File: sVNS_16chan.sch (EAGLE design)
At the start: 56 parts, among them IC2 OPA990IDCKR, IC3 EFM8SB10F8A-A-QFN24EFM8SB10F8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, J1 M50-3631042, J2 M50-3631042, J3 M50-3631042, U1 NT3H2211W0FHKH, U2 LT8410EDC-1#TRMPBF, U3 MUX36S16IRSNR, U4 MUX36S16IRSNR

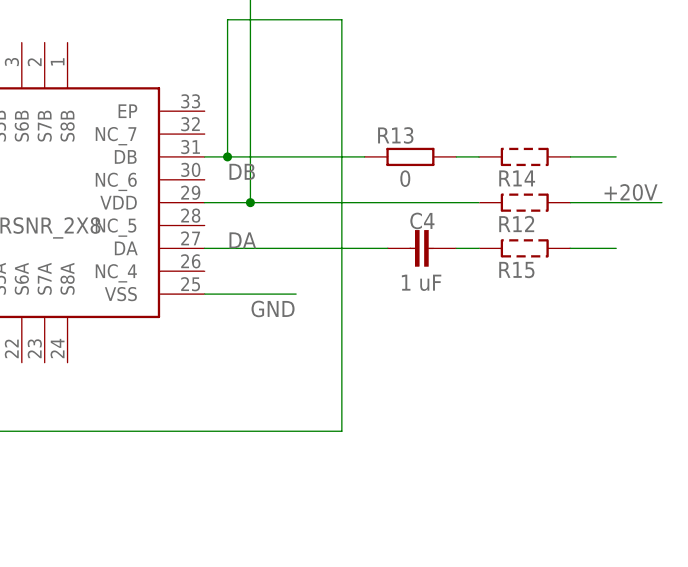
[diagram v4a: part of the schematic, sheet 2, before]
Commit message: Checkpoint 1. Output capacitor changed to 10 uF, form factor 0603.
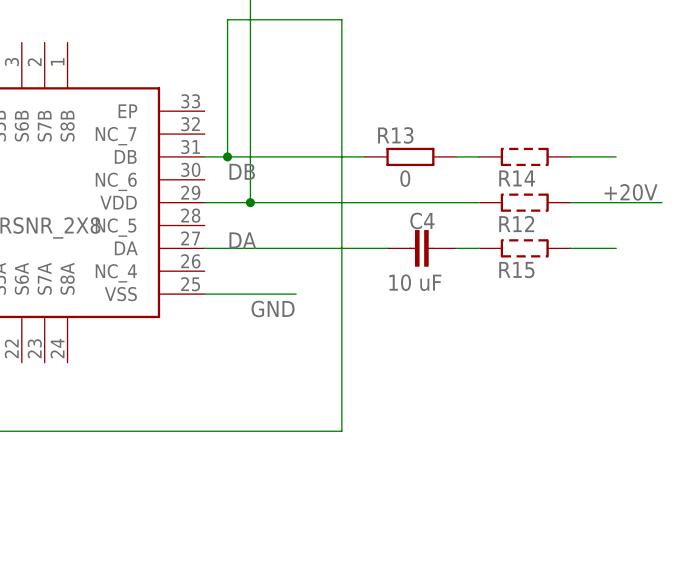
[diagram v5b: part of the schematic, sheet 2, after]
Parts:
- C4: value 1 uF -> 10 uF; device rcl:C-EUC0402 -> rcl:C-EUC0603
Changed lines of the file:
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@@
 <grid distance="0.1" unitdist="inch" unit="inch" style="lines" multiple="1" display="no" altdistance="0.01" altunitdist="inch" altunit="inch"/>
 <layers>
-<layer number="1" name="Top" color="4" fill="1" visible="no" active="no"/>
-<layer number="2" name="Route2" color="16" fill="1" visible="no" active="no"/>
-<layer number="3" name="Route3" color="17" fill="1" visible="no" active="no"/>
-<layer number="4" name="Route4" color="18" fill="1" visible="no" active="no"/>
-<layer number="5" name="Route5" color="19" fill="1" visible="no" active="no"/>
-<layer number="6" name="Route6" color="25" fill="1" visible="no" active="no"/>
-<layer number="7" name="Route7" color="26" fill="1" visible="no" active="no"/>
-<layer number="8" name="Route8" color="27" fill="1" visible="no" active="no"/>
-<layer number="9" name="Route9" color="28" fill="1" visible="no" active="no"/>
-<layer number="10" name="Route10" color="29" fill="1" visible="no" active="no"/>
-<layer number="11" name="Route11" color="30" fill="1" visible="no" active="no"/>
-<layer number="12" name="Route12" color="20" fill="1" visible="no" active="no"/>
-<layer number="13" name="Route13" color="21" fill="1" visible="no" active="no"/>
-<layer number="14" name="Route14" color="22" fill="1" visible="no" active="no"/>
-<layer number="15" name="Route15" color="23" fill="1" visible="no" active="no"/>
-<layer number="16" name="Bottom" color="1" fill="1" visible="no" active="no"/>
-<layer number="17" name="Pads" color="2" fill="1" visible="no" active="no"/>
-<layer number="18" name="Vias" color="2" fill="1" visible="no" active="no"/>
-<layer number="19" name="Unrouted" color="6" fill="1" visible="no" active="no"/>
-<layer number="20" name="Dimension" color="24" fill="1" visible="no" active="no"/>
-<layer number="21" name="tPlace" color="7" fill="1" visible="no" active="no"/>
-<layer number="22" name="bPlace" color="7" fill="1" visible="no" active="no"/>
-<layer number="23" name="tOrigins" color="15" fill="1" visible="no" active="no"/>
-<layer number="24" name="bOrigins" color="15" fill="1" visible="no" active="no"/>
-<layer number="25" name="tNames" color="7" fill="1" visible="no" active="no"/>
-<layer number="26" name="bNames" color="7" fill="1" visible="no" active="no"/>
-<layer number="27" name="tValues" color="7" fill="1" visible="no" active="no"/>
-<layer number="28" name="bValues" color="7" fill="1" visible="no" active="no"/>
+<layer number="1" name="Top" color="4" fill="1" visible="yes" active="no"/>
+<layer number="2" name="Route2" color="16" fill="1" visible="yes" active="no"/>
+<layer number="3" name="Route3" color="17" fill="1" visible="yes" active="no"/>
+<layer number="4" name="Route4" color="18" fill="1" visible="yes" active="no"/>
+<layer number="5" name="Route5" color="19" fill="1" visible="yes" active="no"/>
+<layer number="6" name="Route6" color="25" fill="1" visible="yes" active="no"/>
+<layer number="7" name="Route7" color="26" fill="1" visible="yes" active="no"/>
+<layer number="8" name="Route8" color="27" fill="1" visible="yes" active="no"/>
+<layer number="9" name="Route9" color="28" fill="1" visible="yes" active="no"/>
+<layer number="10" name="Route10" color="29" fill="1" visible="yes" active="no"/>
+<layer number="11" name="Route11" color="30" fill="1" visible="yes" active="no"/>
+<layer number="12" name="Route12" color="20" fill="1" visible="yes" active="no"/>
+<layer number="13" name="Route13" color="21" fill="1" visible="yes" active="no"/>
+<layer number="14" name="Route14" color="22" fill="1" visible="yes" active="no"/>
+<layer number="15" name="Route15" color="23" fill="1" visible="yes" active="no"/>
+<layer number="16" name="Bottom" color="1" fill="1" visible="yes" active="no"/>
+<layer number="17" name="Pads" color="2" fill="1" visible="yes" active="no"/>
+<layer number="18" name="Vias" color="2" fill="1" visible="yes" active="no"/>
+<layer number="19" name="Unrouted" color="6" fill="1" visible="yes" active="no"/>
+<layer number="20" name="Dimension" color="24" fill="1" visible="yes" active="no"/>
+<layer number="21" name="tPlace" color="7" fill="1" visible="yes" active="no"/>
+<layer number="22" name="bPlace" color="7" fill="1" visible="yes" active="no"/>
+<layer number="23" name="tOrigins" color="15" fill="1" visible="yes" active="no"/>
+<layer number="24" name="bOrigins" color="15" fill="1" visible="yes" active="no"/>
+<layer number="25" name="tNames" color="7" fill="1" visible="yes" active="no"/>
+<layer number="26" name="bNames" color="7" fill="1" visible="yes" active="no"/>
+<layer number="27" name="tValues" color="7" fill="1" visible="yes" active="no"/>
+<layer number="28" name="bValues" color="7" fill="1" visible="yes" active="no"/>
 <layer number="29" name="tStop" color="7" fill="3" visible="no" active="no"/>
 <layer number="30" name="bStop" color="7" fill="6" visible="no" active="no"/>
@@
 <layer number="35" name="tGlue" color="7" fill="4" visible="no" active="no"/>
 <layer number="36" name="bGlue" color="7" fill="5" visible="no" active="no"/>
-<layer number="37" name="tTest" color="7" fill="1" visible="no" active="no"/>
-<layer number="38" name="bTest" color="7" fill="1" visible="no" active="no"/>
+<layer number="37" name="tTest" color="7" fill="1" visible="yes" active="no"/>
+<layer number="38" name="bTest" color="7" fill="1" visible="yes" active="no"/>
 <layer number="39" name="tKeepout" color="4" fill="11" visible="no" active="no"/>
 <layer number="40" name="bKeepout" color="1" fill="11" visible="no" active="no"/>
@@
 <layer number="44" name="Drills" color="7" fill="1" visible="no" active="no"/>
 <layer number="45" name="Holes" color="7" fill="1" visible="no" active="no"/>
-<layer number="46" name="Milling" color="3" fill="1" visible="no" active="no"/>
-<layer number="47" name="Measures" color="7" fill="1" visible="no" active="no"/>
-<layer number="48" name="Document" color="7" fill="1" visible="no" active="no"/>
-<layer number="49" name="Reference" color="7" fill="1" visible="no" active="no"/>
-<layer number="50" name="dxf" color="7" fill="1" visible="no" active="no"/>
-<layer number="51" name="tDocu" color="7" fill="1" visible="no" active="no"/>
-<layer number="52" name="bDocu" color="7" fill="1" visible="no" active="no"/>
-<layer number="53" name="tGND_GNDA" color="7" fill="9" visible="no" active="no"/>
-<layer number="54" name="bGND_GNDA" color="1" fill="9" visible="no" active="no"/>
-<layer number="56" name="wert" color="7" fill="1" visible="no" active="no"/>
-<layer number="57" name="tCAD" color="7" fill="1" visible="no" active="no"/>
-<layer number="59" name="tCarbon" color="7" fill="1" visible="no" active="no"/>
-<layer number="60" name="bCarbon" color="7" fill="1" visible="no" active="no"/>
+<layer number="46" name="Milling" color="3" fill="1" visible="yes" active="no"/>
+<layer number="47" name="Measures" color="7" fill="1" visible="yes" active="no"/>
+<layer number="48" name="Document" color="7" fill="1" visible="yes" active="no"/>
+<layer number="49" name="Reference" color="7" fill="1" visible="yes" active="no"/>
+<layer number="50" name="dxf" color="7" fill="1" visible="yes" active="no"/>
+<layer number="51" name="tDocu" color="7" fill="1" visible="yes" active="no"/>
+<layer number="52" name="bDocu" color="7" fill="1" visible="yes" active="no"/>
+<layer number="53" name="tGND_GNDA" color="7" fill="9" visible="yes" active="no"/>
+<layer number="54" name="bGND_GNDA" color="1" fill="9" visible="yes" active="no"/>
+<layer number="56" name="wert" color="7" fill="1" visible="yes" active="no"/>
+<layer number="57" name="tCAD" color="7" fill="1" visible="yes" active="no"/>
+<layer number="59" name="tCarbon" color="7" fill="1" visible="yes" active="no"/>
+<layer number="60" name="bCarbon" color="7" fill="1" visible="yes" active="no"/>
 <layer number="88" name="SimResults" color="9" fill="1" visible="yes" active="yes"/>
 <layer number="89" name="SimProbes" color="9" fill="1" visible="yes" active="yes"/>
@@
 <part name="R10" library="rcl" library_urn="urn:adsk.eagle:library:334" deviceset="R-EU_" device="R0402" package3d_urn="urn:adsk.eagle:package:23547/3" value="220k"/>
 <part name="C12" library="rcl" library_urn="urn:adsk.eagle:library:334" deviceset="C-EU" device="C0402" package3d_urn="urn:adsk.eagle:package:23626/2" value="0.1 uF"/>
-<part name="C4" library="rcl" library_urn="urn:adsk.eagle:library:334" deviceset="C-EU" device="C0402" package3d_urn="urn:adsk.eagle:package:23626/2" value="1 uF"/>
+<part name="C4" library="rcl" library_urn="urn:adsk.eagle:library:334" deviceset="C-EU" device="C0603" package3d_urn="urn:adsk.eagle:package:23616/2" value="10 uF"/>
 <part name="R13" library="rcl" library_urn="urn:adsk.eagle:library:334" deviceset="R-EU_" device="R0402" package3d_urn="urn:adsk.eagle:package:23547/3" value="0"/>
 <part name="C11" library="rcl" library_urn="urn:adsk.eagle:library:334" deviceset="C-EU" device="C0402" package3d_urn="urn:adsk.eagle:package:23626/2" value="0.1 uF"/>

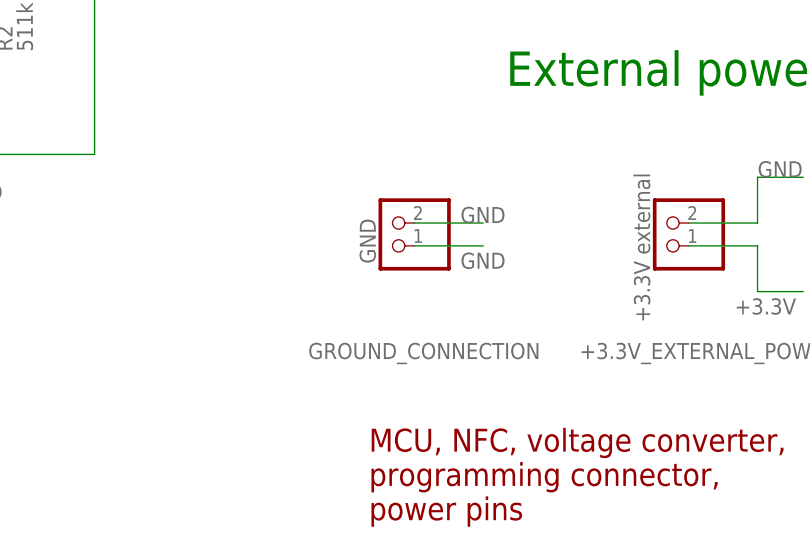
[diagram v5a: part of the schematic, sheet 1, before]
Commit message: Checkpoint 2. Minor changes and optimizations for the manufacturing. Output cap changed to 10 uF. Prepared for PCBway if this version considered to be manufactured.
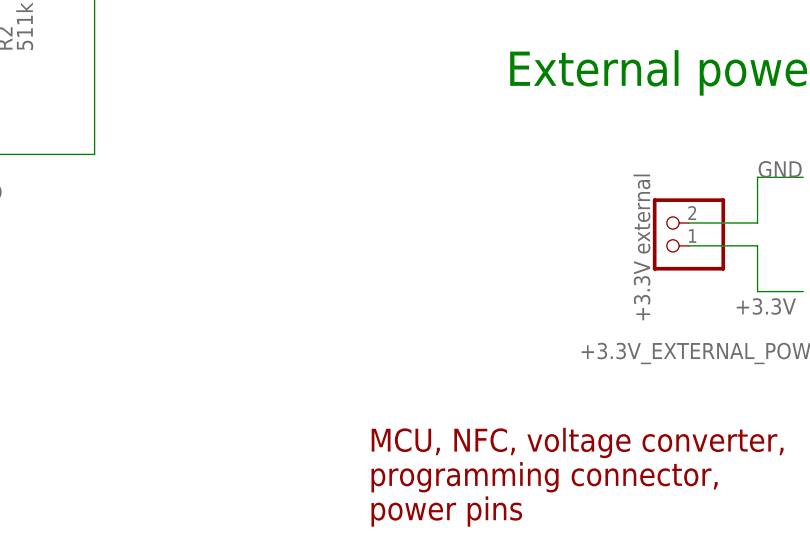
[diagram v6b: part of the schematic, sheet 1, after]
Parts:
- removed GROUND_CONNECTION: GND, pinhead:PINHD-1X2
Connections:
- net GND: no longer GROUND_CONNECTION.1, GROUND_CONNECTION.2
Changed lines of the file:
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@@
 <grid distance="0.1" unitdist="inch" unit="inch" style="lines" multiple="1" display="no" altdistance="0.01" altunitdist="inch" altunit="inch"/>
 <layers>
-<layer number="1" name="Top" color="4" fill="1" visible="yes" active="no"/>
-<layer number="2" name="Route2" color="16" fill="1" visible="yes" active="no"/>
-<layer number="3" name="Route3" color="17" fill="1" visible="yes" active="no"/>
-<layer number="4" name="Route4" color="18" fill="1" visible="yes" active="no"/>
-<layer number="5" name="Route5" color="19" fill="1" visible="yes" active="no"/>
-<layer number="6" name="Route6" color="25" fill="1" visible="yes" active="no"/>
-<layer number="7" name="Route7" color="26" fill="1" visible="yes" active="no"/>
-<layer number="8" name="Route8" color="27" fill="1" visible="yes" active="no"/>
-<layer number="9" name="Route9" color="28" fill="1" visible="yes" active="no"/>
-<layer number="10" name="Route10" color="29" fill="1" visible="yes" active="no"/>
-<layer number="11" name="Route11" color="30" fill="1" visible="yes" active="no"/>
-<layer number="12" name="Route12" color="20" fill="1" visible="yes" active="no"/>
-<layer number="13" name="Route13" color="21" fill="1" visible="yes" active="no"/>
-<layer number="14" name="Route14" color="22" fill="1" visible="yes" active="no"/>
-<layer number="15" name="Route15" color="23" fill="1" visible="yes" active="no"/>
-<layer number="16" name="Bottom" color="1" fill="1" visible="yes" active="no"/>
-<layer number="17" name="Pads" color="2" fill="1" visible="yes" active="no"/>
-<layer number="18" name="Vias" color="2" fill="1" visible="yes" active="no"/>
-<layer number="19" name="Unrouted" color="6" fill="1" visible="yes" active="no"/>
-<layer number="20" name="Dimension" color="24" fill="1" visible="yes" active="no"/>
-<layer number="21" name="tPlace" color="7" fill="1" visible="yes" active="no"/>
-<layer number="22" name="bPlace" color="7" fill="1" visible="yes" active="no"/>
-<layer number="23" name="tOrigins" color="15" fill="1" visible="yes" active="no"/>
-<layer number="24" name="bOrigins" color="15" fill="1" visible="yes" active="no"/>
-<layer number="25" name="tNames" color="7" fill="1" visible="yes" active="no"/>
-<layer number="26" name="bNames" color="7" fill="1" visible="yes" active="no"/>
-<layer number="27" name="tValues" color="7" fill="1" visible="yes" active="no"/>
-<layer number="28" name="bValues" color="7" fill="1" visible="yes" active="no"/>
+<layer number="1" name="Top" color="4" fill="1" visible="no" active="no"/>
+<layer number="2" name="Route2" color="16" fill="1" visible="no" active="no"/>
+<layer number="3" name="Route3" color="17" fill="1" visible="no" active="no"/>
+<layer number="4" name="Route4" color="18" fill="1" visible="no" active="no"/>
+<layer number="5" name="Route5" color="19" fill="1" visible="no" active="no"/>
+<layer number="6" name="Route6" color="25" fill="1" visible="no" active="no"/>
+<layer number="7" name="Route7" color="26" fill="1" visible="no" active="no"/>
+<layer number="8" name="Route8" color="27" fill="1" visible="no" active="no"/>
+<layer number="9" name="Route9" color="28" fill="1" visible="no" active="no"/>
+<layer number="10" name="Route10" color="29" fill="1" visible="no" active="no"/>
+<layer number="11" name="Route11" color="30" fill="1" visible="no" active="no"/>
+<layer number="12" name="Route12" color="20" fill="1" visible="no" active="no"/>
+<layer number="13" name="Route13" color="21" fill="1" visible="no" active="no"/>
+<layer number="14" name="Route14" color="22" fill="1" visible="no" active="no"/>
+<layer number="15" name="Route15" color="23" fill="1" visible="no" active="no"/>
+<layer number="16" name="Bottom" color="1" fill="1" visible="no" active="no"/>
+<layer number="17" name="Pads" color="2" fill="1" visible="no" active="no"/>
+<layer number="18" name="Vias" color="2" fill="1" visible="no" active="no"/>
+<layer number="19" name="Unrouted" color="6" fill="1" visible="no" active="no"/>
+<layer number="20" name="Dimension" color="24" fill="1" visible="no" active="no"/>
+<layer number="21" name="tPlace" color="7" fill="1" visible="no" active="no"/>
+<layer number="22" name="bPlace" color="7" fill="1" visible="no" active="no"/>
+<layer number="23" name="tOrigins" color="15" fill="1" visible="no" active="no"/>
+<layer number="24" name="bOrigins" color="15" fill="1" visible="no" active="no"/>
+<layer number="25" name="tNames" color="7" fill="1" visible="no" active="no"/>
+<layer number="26" name="bNames" color="7" fill="1" visible="no" active="no"/>
+<layer number="27" name="tValues" color="7" fill="1" visible="no" active="no"/>
+<layer number="28" name="bValues" color="7" fill="1" visible="no" active="no"/>
 <layer number="29" name="tStop" color="7" fill="3" visible="no" active="no"/>
 <layer number="30" name="bStop" color="7" fill="6" visible="no" active="no"/>
@@
 <layer number="35" name="tGlue" color="7" fill="4" visible="no" active="no"/>
 <layer number="36" name="bGlue" color="7" fill="5" visible="no" active="no"/>
-<layer number="37" name="tTest" color="7" fill="1" visible="yes" active="no"/>
-<layer number="38" name="bTest" color="7" fill="1" visible="yes" active="no"/>
+<layer number="37" name="tTest" color="7" fill="1" visible="no" active="no"/>
+<layer number="38" name="bTest" color="7" fill="1" visible="no" active="no"/>
 <layer number="39" name="tKeepout" color="4" fill="11" visible="no" active="no"/>
 <layer number="40" name="bKeepout" color="1" fill="11" visible="no" active="no"/>
@@
 <layer number="44" name="Drills" color="7" fill="1" visible="no" active="no"/>
 <layer number="45" name="Holes" color="7" fill="1" visible="no" active="no"/>
-<layer number="46" name="Milling" color="3" fill="1" visible="yes" active="no"/>
-<layer number="47" name="Measures" color="7" fill="1" visible="yes" active="no"/>
-<layer number="48" name="Document" color="7" fill="1" visible="yes" active="no"/>
-<layer number="49" name="Reference" color="7" fill="1" visible="yes" active="no"/>
-<layer number="50" name="dxf" color="7" fill="1" visible="yes" active="no"/>
-<layer number="51" name="tDocu" color="7" fill="1" visible="yes" active="no"/>
-<layer number="52" name="bDocu" color="7" fill="1" visible="yes" active="no"/>
-<layer number="53" name="tGND_GNDA" color="7" fill="9" visible="yes" active="no"/>
-<layer number="54" name="bGND_GNDA" color="1" fill="9" visible="yes" active="no"/>
-<layer number="56" name="wert" color="7" fill="1" visible="yes" active="no"/>
-<layer number="57" name="tCAD" color="7" fill="1" visible="yes" active="no"/>
-<layer number="59" name="tCarbon" color="7" fill="1" visible="yes" active="no"/>
-<layer number="60" name="bCarbon" color="7" fill="1" visible="yes" active="no"/>
+<layer number="46" name="Milling" color="3" fill="1" visible="no" active="no"/>
+<layer number="47" name="Measures" color="7" fill="1" visible="no" active="no"/>
+<layer number="48" name="Document" color="7" fill="1" visible="no" active="no"/>
+<layer number="49" name="Reference" color="7" fill="1" visible="no" active="no"/>
+<layer number="50" name="dxf" color="7" fill="1" visible="no" active="no"/>
+<layer number="51" name="tDocu" color="7" fill="1" visible="no" active="no"/>
+<layer number="52" name="bDocu" color="7" fill="1" visible="no" active="no"/>
+<layer number="53" name="tGND_GNDA" color="7" fill="9" visible="no" active="no"/>
+<layer number="54" name="bGND_GNDA" color="1" fill="9" visible="no" active="no"/>
+<layer number="56" name="wert" color="7" fill="1" visible="no" active="no"/>
+<layer number="57" name="tCAD" color="7" fill="1" visible="no" active="no"/>
+<layer number="59" name="tCarbon" color="7" fill="1" visible="no" active="no"/>
+<layer number="60" name="bCarbon" color="7" fill="1" visible="no" active="no"/>
 <layer number="88" name="SimResults" color="9" fill="1" visible="yes" active="yes"/>
 <layer number="89" name="SimProbes" color="9" fill="1" visible="yes" active="yes"/>
@@
 <part name="C5" library="rcl" library_urn="urn:adsk.eagle:library:334" deviceset="C-EU" device="C0402" package3d_urn="urn:adsk.eagle:package:23626/2" value="0.1 uF"/>
 <part name="C10" library="rcl" library_urn="urn:adsk.eagle:library:334" deviceset="C-EU" device="C0402" package3d_urn="urn:adsk.eagle:package:23626/2" value="0.1 uF"/>
-<part name="GROUND_CONNECTION" library="pinhead" library_urn="urn:adsk.eagle:library:325" deviceset="PINHD-1X2" device="" package3d_urn="urn:adsk.eagle:package:22435/2" value="GND"/>
 <part name="DEBUG_N_2510_SOCKET" library="N2510-6002RB" deviceset="N2510-6002RB" device=""/>
 <part name="C14" library="rcl" library_urn="urn:adsk.eagle:library:334" deviceset="C-EU" device="C0402" package3d_urn="urn:adsk.eagle:package:23626/2" value="0.1 uF"/>
@@
 <attribute name="VALUE" x="41.656" y="78.359" size="1.778" layer="96" rot="R180"/>
 </instance>
-<instance part="GROUND_CONNECTION" gate="G$1" x="167.64" y="43.18" smashed="yes" rot="R180">
-<attribute name="NAME" x="184.15" y="29.845" size="1.778" layer="95" rot="R180"/>
-<attribute name="VALUE" x="164.084" y="43.688" size="1.778" layer="96" rot="R270"/>
-</instance>
 <instance part="DEBUG_N_2510_SOCKET" gate="A" x="226.06" y="96.52" smashed="yes">
 <attribute name="NAME" x="214.9856" y="68.8086" size="2.0828" layer="95" ratio="6" rot="SR0"/>
@@
 </segment>
 <segment>
-<pinref part="GROUND_CONNECTION" gate="G$1" pin="1"/>
-<wire x1="170.18" y1="40.64" x2="177.8" y2="40.64" width="0.1524" layer="91"/>
-<label x="175.26" y="38.1" size="1.778" layer="95"/>
-</segment>
-<segment>
-<pinref part="GROUND_CONNECTION" gate="G$1" pin="2"/>
-<wire x1="170.18" y1="43.18" x2="177.8" y2="43.18" width="0.1524" layer="91"/>
-<label x="175.26" y="43.18" size="1.778" layer="95"/>
-</segment>
-<segment>
